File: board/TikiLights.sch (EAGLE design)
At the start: 41 parts, among them IC1 AZ1117EH-3.3TRG1, SW1 ROTARTY_ENCODER, SW2 ROTARTY_ENCODER, SW3 ENCODER_SW1-PEC12, SW4 ENCODER_SW1-PEC12

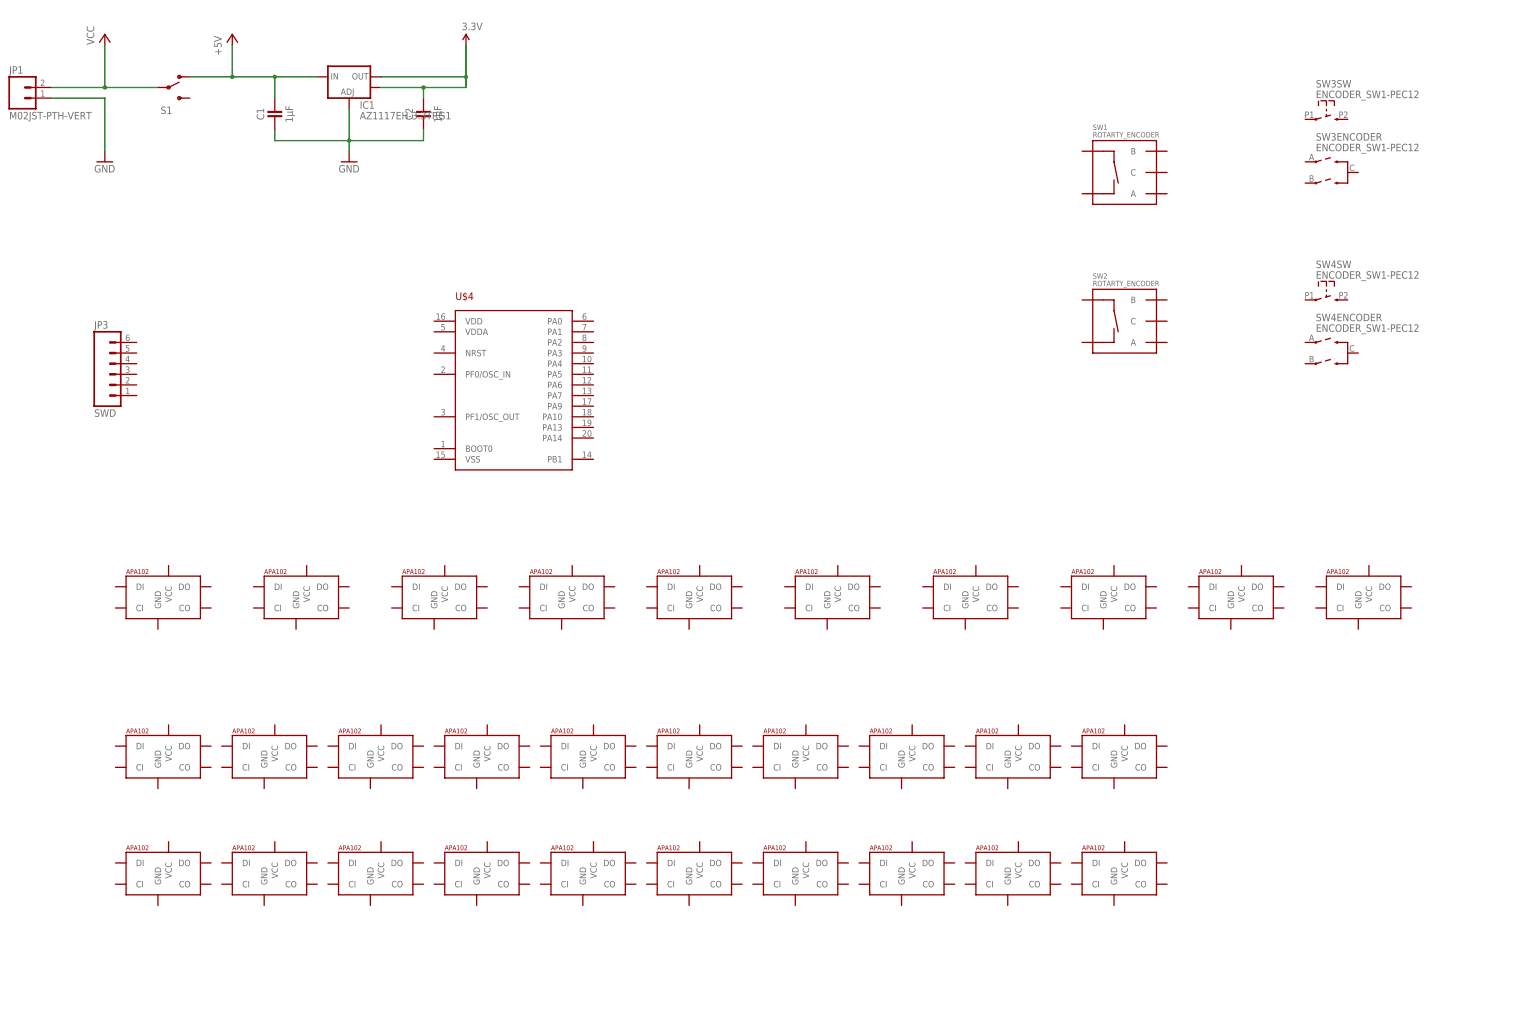
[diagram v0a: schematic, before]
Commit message: Schematic is finished. Screw holes added. Need board layout and updated CAD model for dimensions.
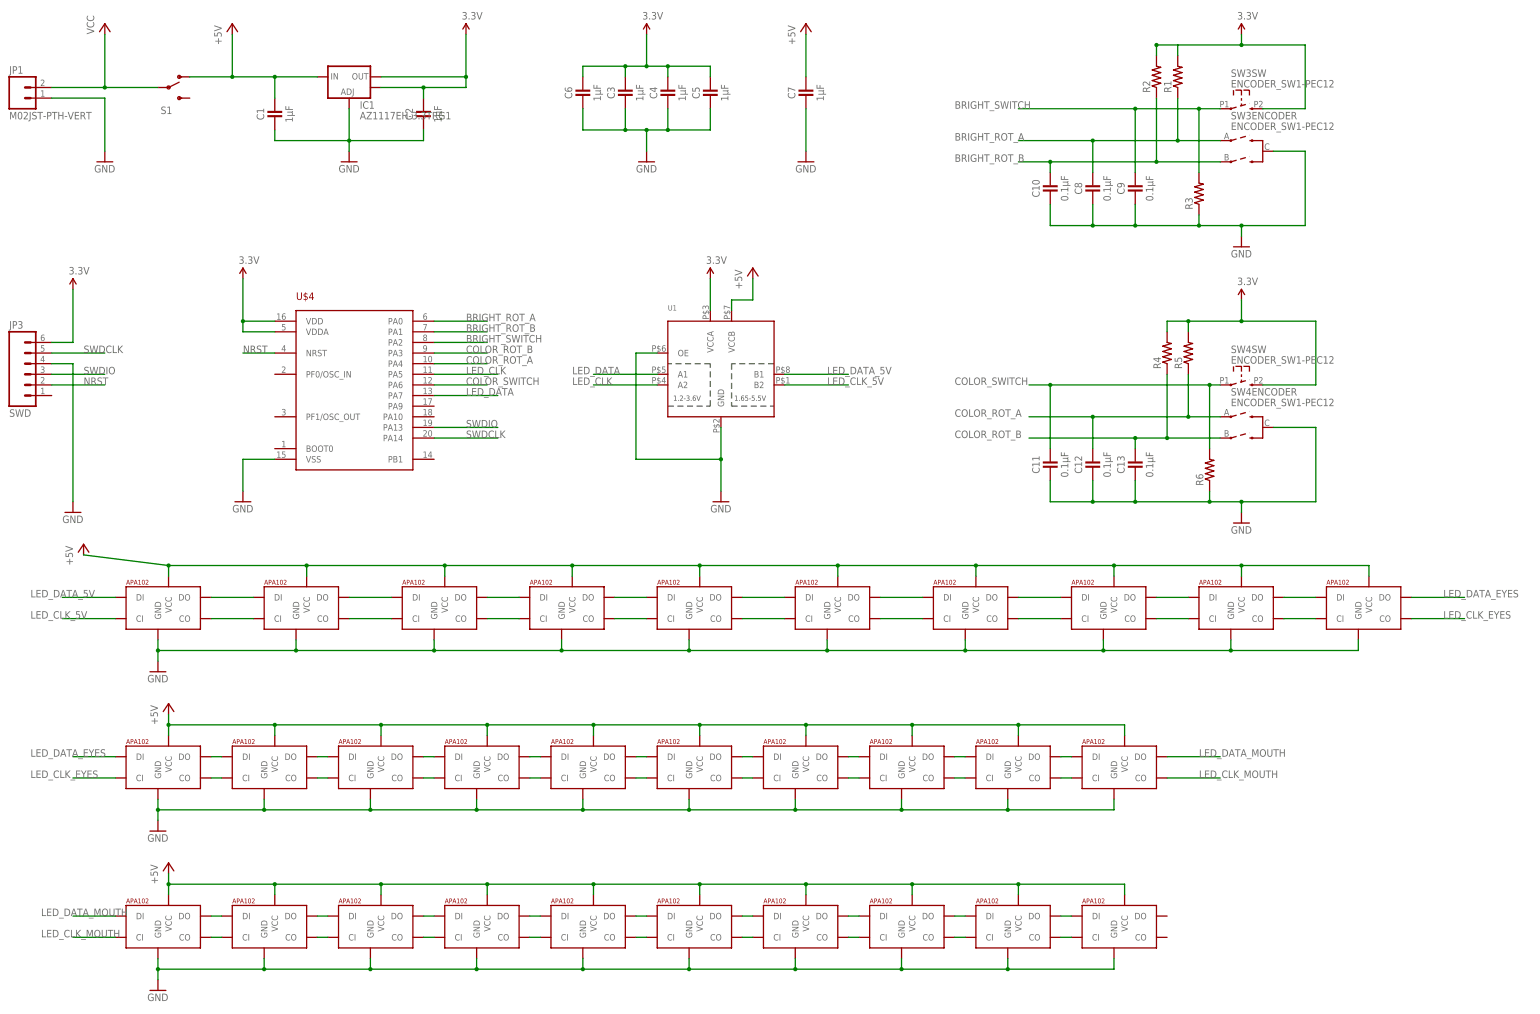
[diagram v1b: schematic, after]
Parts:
- removed SW1, SW2: ROTARTY_ENCODER, SparkFun-Electromechanical:ROTARTY_ENCODER
- added C10, C11, C12, C13, C8, C9: 0.1µF, passives:CAPACITOR0603_CAP
- added C3, C4, C5, C6, C7: 1µF, passives:CAPACITOR0603_CAP
- added R1, R2, R3, R4, R5, R6: (no value), SparkFun-Resistors:RESISTOR0603
- added U1: (no value), adafruit:TXS0102
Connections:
- new net BRIGHT_ROT_A: C8.1, R1.1, SW3ENCODER.A, U$4.PA0
- new net BRIGHT_ROT_B: C10.1, R2.1, SW3ENCODER.B, U$4.PA1
- new net BRIGHT_SWITCH: C9.1, R3.2, SW3SW.1, U$4.PA2
- new net COLOR_ROT_A: C12.1, R5.1, SW4ENCODER.A, U$4.PA4
- new net COLOR_ROT_B: C13.1, R4.1, SW4ENCODER.B, U$4.PA3
- new net COLOR_SWITCH: C11.1, R6.2, SW4SW.1, U$4.PA6
- new net LED_CLK: U$4.PA5, U1.A2
- new net LED_CLK_5V: U$1.CI, U1.B2
- new net LED_CLK_EYES: U$31.CO, U$7.CI
- new net LED_CLK_MOUTH: U$16.CO, U$17.CI
- new net LED_DATA: U$4.PA7, U1.A1
- new net LED_DATA_5V: U$1.DI, U1.B1
- new net LED_DATA_EYES: U$31.DO, U$7.DI
- new net LED_DATA_MOUTH: U$16.DO, U$17.DI
- new net N$14: U$2.DO, U$3.DI
- new net N$15: U$2.CO, U$3.CI
- new net N$16: U$3.DO, U$5.DI
- new net N$17: U$3.CO, U$5.CI
- new net N$18: U$5.DO, U$6.DI
- new net N$19: U$5.CO, U$6.CI
- new net N$20: U$27.DI, U$6.DO
- new net N$21: U$27.CI, U$6.CO
- new net N$22: U$27.DO, U$28.DI
- new net N$23: U$27.CO, U$28.CI
- new net N$24: U$28.DO, U$29.DI
- new net N$25: U$28.CO, U$29.CI
- new net N$26: U$29.DO, U$30.DI
- new net N$27: U$29.CO, U$30.CI
- new net N$28: U$30.DO, U$31.DI
- new net N$29: U$30.CO, U$31.CI
- new net N$34: U$7.CO, U$8.CI
- new net N$35: U$7.DO, U$8.DI
- new net N$36: U$8.DO, U$9.DI
- new net N$37: U$8.CO, U$9.CI
- new net N$38: U$10.DI, U$9.DO
- new net N$39: U$10.CI, U$9.CO
- new net N$40: U$10.DO, U$11.DI
- new net N$41: U$10.CO, U$11.CI
- new net N$42: U$11.DO, U$12.DI
- new net N$43: U$11.CO, U$12.CI
- new net N$44: U$12.DO, U$13.DI
- new net N$45: U$12.CO, U$13.CI
- new net N$46: U$13.DO, U$14.DI
- new net N$47: U$13.CO, U$14.CI
- new net N$48: U$14.DO, U$15.DI
- new net N$49: U$14.CO, U$15.CI
- new net N$50: U$15.CO, U$16.CI
- new net N$51: U$15.DO, U$16.DI
- new net N$56: U$17.DO, U$18.DI
- new net N$57: U$17.CO, U$18.CI
- new net N$58: U$18.DO, U$19.DI
- new net N$59: U$18.CO, U$19.CI
- new net N$60: U$19.DO, U$20.DI
- new net N$61: U$19.CO, U$20.CI
- new net N$62: U$20.DO, U$21.DI
- new net N$63: U$20.CO, U$21.CI
- new net N$64: U$21.DO, U$22.DI
- new net N$65: U$21.CO, U$22.CI
- new net N$66: U$22.DO, U$23.DI
- new net N$67: U$22.CO, U$23.CI
- new net N$68: U$23.DO, U$24.DI
- new net N$69: U$23.CO, U$24.CI
- new net N$7: U$1.DO, U$2.DI
- new net N$70: U$24.DO, U$25.DI
- new net N$71: U$24.CO, U$25.CI
- new net N$72: U$25.DO, U$26.DI
- new net N$73: U$25.CO, U$26.CI
- new net N$9: U$1.CO, U$2.CI
- new net NRST: JP3.2, U$4.NRST
- new net SWDCLK: JP3.5, U$4.PA14
- new net SWDIO: JP3.3, U$4.PA13
- net +5V: now also C7.1, U$1.VCC, U$10.VCC, U$11.VCC, U$12.VCC, U$13.VCC, U$14.VCC, U$15.VCC, U$16.VCC, U$17.VCC, U$18.VCC, U$19.VCC, U$2.VCC, U$20.VCC, U$21.VCC, U$22.VCC, U$23.VCC, U$24.VCC, U$25.VCC, U$26.VCC, U$27.VCC, U$28.VCC, U$29.VCC, U$3.VCC, U$30.VCC, U$31.VCC, U$5.VCC, U$6.VCC, U$7.VCC, U$8.VCC, U$9.VCC, U1.VCCB
- net 3.3V: now also C3.1, C4.1, C5.1, C6.1, JP3.6, R1.2, R2.2, R4.2, R5.2, SW3SW.2, SW4SW.2, U$4.VDD, U$4.VDDA, U1.VCCA
- net GND: now also C10.2, C11.2, C12.2, C13.2, C3.2, C4.2, C5.2, C6.2, C7.2, C8.2, C9.2, JP3.4, R3.1, R6.1, SW3ENCODER.C, SW4ENCODER.C, U$1.GND, U$10.GND, U$11.GND, U$12.GND, U$13.GND, U$14.GND, U$15.GND, U$16.GND, U$17.GND, U$18.GND, U$19.GND, U$2.GND, U$20.GND, U$21.GND, U$22.GND, U$23.GND, U$24.GND, U$25.GND, U$26.GND, U$27.GND, U$28.GND, U$29.GND, U$3.GND, U$30.GND, U$31.GND, U$4.VSS, U$5.GND, U$6.GND, U$7.GND, U$8.GND, U$9.GND, U1.GND, U1.OE
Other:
- moved on the sheet: JP3, SW3ENCODER, SW3SW, SW4ENCODER, SW4SW, U$4

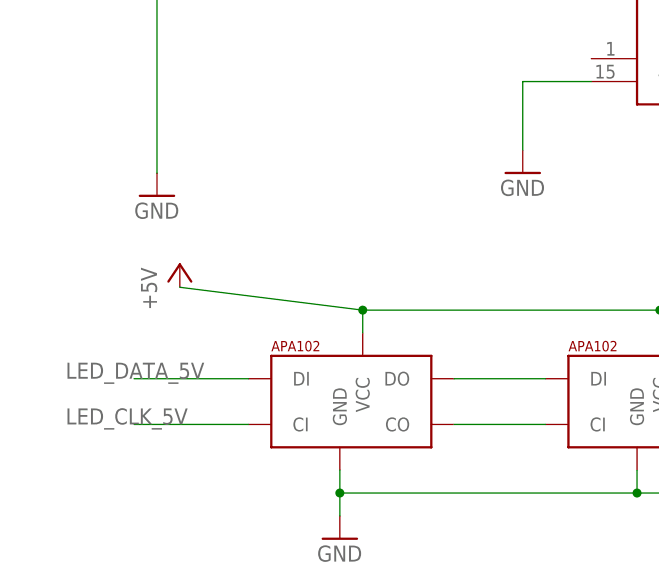
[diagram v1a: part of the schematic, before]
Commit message: Updating board to fit resized mask. Battery pack now fits and everything is in place for routing. Mask still needs a hook, and board needs a message.
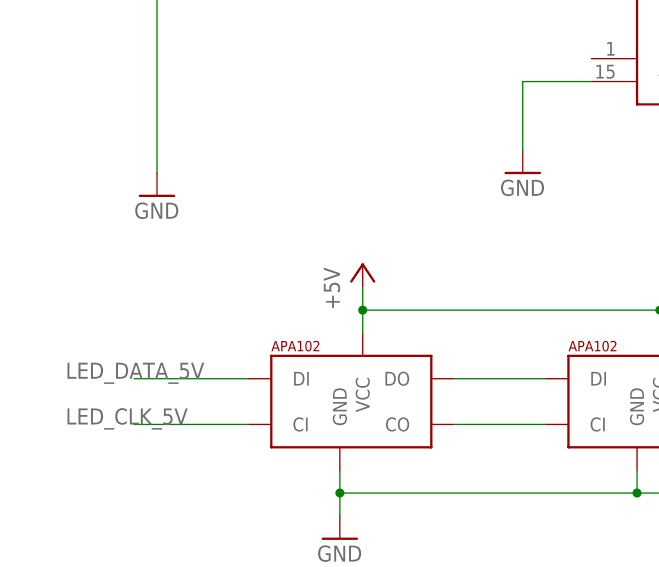
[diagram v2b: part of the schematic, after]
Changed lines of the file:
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@@
 <instance part="GND6" gate="1" x="27.94" y="129.54"/>
 <instance part="SUPPLY4" gate="G$1" x="27.94" y="182.88"/>
-<instance part="P+4" gate="1" x="30.48" y="121.92"/>
+<instance part="P+4" gate="1" x="50.8" y="121.92"/>
 <instance part="GND7" gate="1" x="48.26" y="91.44"/>
 <instance part="P+5" gate="1" x="50.8" y="83.82"/>
@@
 <wire x1="50.8" y1="114.3" x2="50.8" y2="116.84" width="0.1524" layer="91"/>
 <pinref part="U$2" gate="G$1" pin="VCC"/>
-<wire x1="50.8" y1="116.84" x2="30.48" y2="119.38" width="0.1524" layer="91"/>
+<wire x1="50.8" y1="116.84" x2="50.8" y2="119.38" width="0.1524" layer="91"/>
 <wire x1="83.82" y1="114.3" x2="83.82" y2="116.84" width="0.1524" layer="91"/>
 <wire x1="83.82" y1="116.84" x2="50.8" y2="116.84" width="0.1524" layer="91"/>

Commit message: Submitting tikilights v1. Both board and cad. Hope I didn't forget anything!
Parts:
- R1, R2, R3, R4, R5, R6: value (none) -> 10k
- S1: value (none) -> SPDT
- U1: value (none) -> AZ1117E
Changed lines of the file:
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@@
 <part name="U$30" library="jos-ph" deviceset="APA102" device="2020"/>
 <part name="U$31" library="jos-ph" deviceset="APA102" device="2020"/>
-<part name="S1" library="SparkFun-Electromechanical" deviceset="SWITCH-SPDT" device="PTH"/>
+<part name="S1" library="SparkFun-Electromechanical" deviceset="SWITCH-SPDT" device="PTH" value="SPDT"/>
 <part name="P+1" library="supply1" deviceset="+5V" device=""/>
 <part name="GND1" library="supply1" deviceset="GND" device=""/>
@@
 <part name="P+6" library="supply1" deviceset="+5V" device=""/>
 <part name="GND9" library="supply1" deviceset="GND" device=""/>
-<part name="U1" library="adafruit" deviceset="TXS0102" device=""/>
+<part name="U1" library="adafruit" deviceset="TXS0102" device="" value="AZ1117E"/>
 <part name="SUPPLY5" library="SparkFun-Aesthetics" deviceset="3.3V" device=""/>
 <part name="P+7" library="supply1" deviceset="+5V" device=""/>
@@
 <part name="C9" library="passives" deviceset="CAPACITOR" device="0603_CAP" value="0.1µF"/>
 <part name="C10" library="passives" deviceset="CAPACITOR" device="0603_CAP" value="0.1µF"/>
-<part name="R1" library="SparkFun-Resistors" deviceset="RESISTOR" device="0603"/>
-<part name="R2" library="SparkFun-Resistors" deviceset="RESISTOR" device="0603"/>
-<part name="R3" library="SparkFun-Resistors" deviceset="RESISTOR" device="0603"/>
+<part name="R1" library="SparkFun-Resistors" deviceset="RESISTOR" device="0603" value="10k"/>
+<part name="R2" library="SparkFun-Resistors" deviceset="RESISTOR" device="0603" value="10k"/>
+<part name="R3" library="SparkFun-Resistors" deviceset="RESISTOR" device="0603" value="10k"/>
 <part name="SUPPLY7" library="SparkFun-Aesthetics" deviceset="3.3V" device=""/>
 <part name="GND12" library="supply1" deviceset="GND" device=""/>
-<part name="R4" library="SparkFun-Resistors" deviceset="RESISTOR" device="0603"/>
-<part name="R5" library="SparkFun-Resistors" deviceset="RESISTOR" device="0603"/>
-<part name="R6" library="SparkFun-Resistors" deviceset="RESISTOR" device="0603"/>
+<part name="R4" library="SparkFun-Resistors" deviceset="RESISTOR" device="0603" value="10k"/>
+<part name="R5" library="SparkFun-Resistors" deviceset="RESISTOR" device="0603" value="10k"/>
+<part name="R6" library="SparkFun-Resistors" deviceset="RESISTOR" device="0603" value="10k"/>
 <part name="C11" library="passives" deviceset="CAPACITOR" device="0603_CAP" value="0.1µF"/>
 <part name="C12" library="passives" deviceset="CAPACITOR" device="0603_CAP" value="0.1µF"/>
@@
 <wire x1="322.58" y1="241.3" x2="307.34" y2="241.3" width="0.1524" layer="91"/>
 <wire x1="307.34" y1="241.3" x2="307.34" y2="243.84" width="0.1524" layer="91"/>
-<pinref part="R2" gate="G$1" pin="2"/>
-<wire x1="287.02" y1="238.76" x2="287.02" y2="241.3" width="0.1524" layer="91"/>
 <junction x="307.34" y="241.3"/>
 <pinref part="R1" gate="G$1" pin="2"/>
 <wire x1="292.1" y1="241.3" x2="307.34" y2="241.3" width="0.1524" layer="91"/>
 <wire x1="292.1" y1="238.76" x2="292.1" y2="241.3" width="0.1524" layer="91"/>
-<wire x1="292.1" y1="241.3" x2="287.02" y2="241.3" width="0.1524" layer="91"/>
-<junction x="287.02" y="241.3"/>
-</segment>
-<segment>
+<pinref part="R2" gate="G$1" pin="2"/>
+<wire x1="287.02" y1="238.76" x2="287.02" y2="241.3" width="0.1524" layer="91"/>
+<wire x1="287.02" y1="241.3" x2="292.1" y2="241.3" width="0.1524" layer="91"/>
+<junction x="292.1" y="241.3"/>
+</segment>
+<segment>
